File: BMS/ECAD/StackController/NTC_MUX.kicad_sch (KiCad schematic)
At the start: 10 parts, among them U2 TMUX1309A, U3 TMUX1309A

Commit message: finish V09 of stack controller and HV indicator
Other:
- company: (none) -> Lukas Deeken Elektronik
- title: (none) -> Stack Controller
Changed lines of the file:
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@@
 	(generator_version "9.0")
 	(paper "A4")
+	(title_block
+		(title "Stack Controller")
+		(date "2026-02-27")
+		(rev "1.0")
+		(company "Lukas Deeken Elektronik")
+	)
 	(text_box "R gegen GND ist zur Diagnose für 10k NTC B3950 TNom25°C\n866k = -49,96°C\n887k = -50,26°C\n909k = -50,57°C\n931k = -50,87°C\n953k = -51,16°C\n"
 		(exclude_from_sim no)

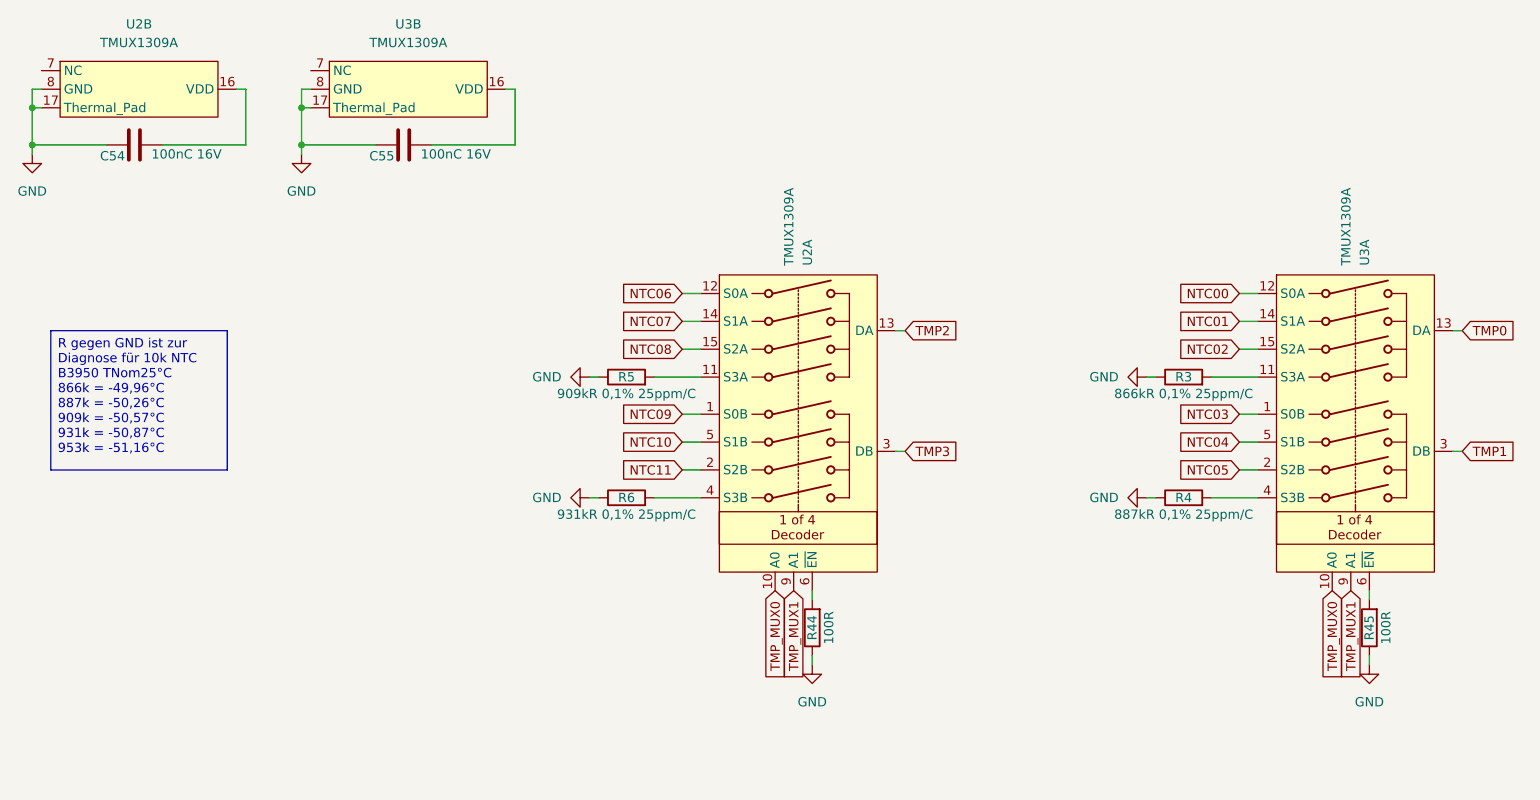
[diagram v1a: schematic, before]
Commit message: started layout BMS slave
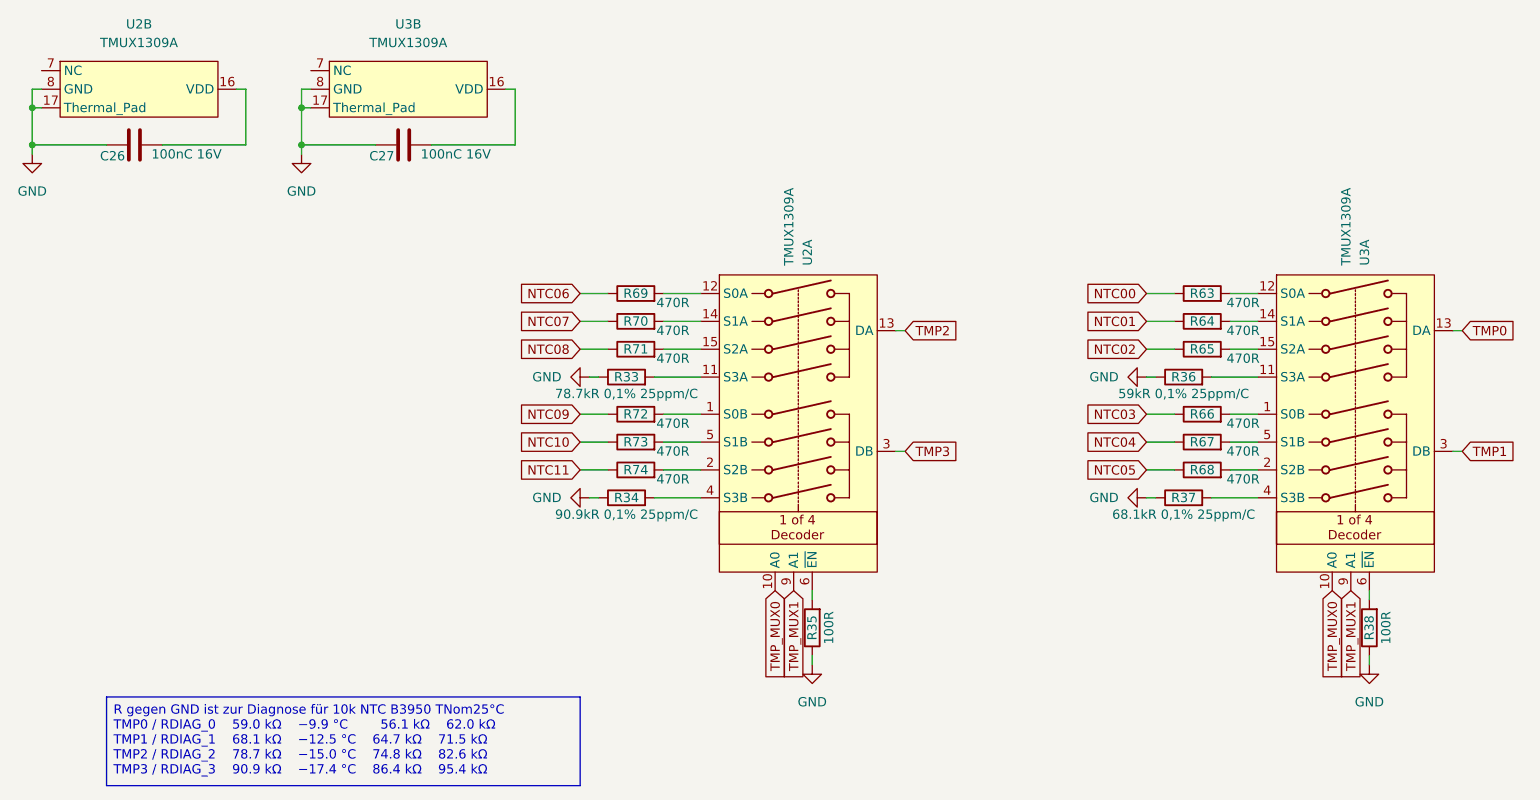
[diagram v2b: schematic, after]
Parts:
- added R63, R64, R65, R66, R67, R68, R69, R70, R71, R72, R73, R74: 470R, Resistor_SMD:R_0603_1608Metric, symbol Device:R
- R33: renamed from R5; value 909kR 0,1% 25ppm/C -> 78.7kR 0,1% 25ppm/C
- R34: renamed from R6; value 931kR 0,1% 25ppm/C -> 90.9kR 0,1% 25ppm/C
- R36: renamed from R3; value 866kR 0,1% 25ppm/C -> 59kR 0,1% 25ppm/C
- R37: renamed from R4; value 887kR 0,1% 25ppm/C -> 68.1kR 0,1% 25ppm/C
- U2, U3: footprint (none) -> Package_SO:TSSOP-16_4.4x5mm_P0.65mm
- renumbered C54 to C26, C55 to C27, R44 to R35, R45 to R38
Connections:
- net NTC00: now also R63.1; no longer U3.12 (S0A)
- net NTC01: now also R64.1; no longer U3.14 (S1A)
- net NTC02: now also R65.1; no longer U3.15 (S2A)
- net NTC03: now also R66.1; no longer U3.1 (S0B)
- net NTC04: now also R67.1; no longer U3.5 (S1B)
- net NTC05: now also R68.1; no longer U3.2 (S2B)
- net NTC06: now also R69.1; no longer U2.12 (S0A)
- net NTC07: now also R70.1; no longer U2.14 (S1A)
- net NTC08: now also R71.1; no longer U2.15 (S2A)
- net NTC09: now also R72.1; no longer U2.1 (S0B)
- net NTC10: now also R73.1; no longer U2.5 (S1B)
- net NTC11: now also R74.1; no longer U2.2 (S2B)
- new net: R73.2, U2.5 (S1B)
- new net: R66.2, U3.1 (S0B)
- new net: R69.2, U2.12 (S0A)
- new net: R67.2, U3.5 (S1B)
- new net: R68.2, U3.2 (S2B)
- new net: R63.2, U3.12 (S0A)
- new net: R64.2, U3.14 (S1A)
- new net: R65.2, U3.15 (S2A)
- new net: R71.2, U2.15 (S2A)
- new net: R72.2, U2.1 (S0B)
- new net: R70.2, U2.14 (S1A)
- new net: R74.2, U2.2 (S2B)
